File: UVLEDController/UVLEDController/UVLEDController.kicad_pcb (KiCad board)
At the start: 2 copper layers, 56 x 80 mm, 13 parts, among them J1-LED1 Screw_Terminal_01x02, J2-PWR1 Screw_Terminal_01x02, J3 Conn_01x04_Male, Q1 Q_NMOS_GDS

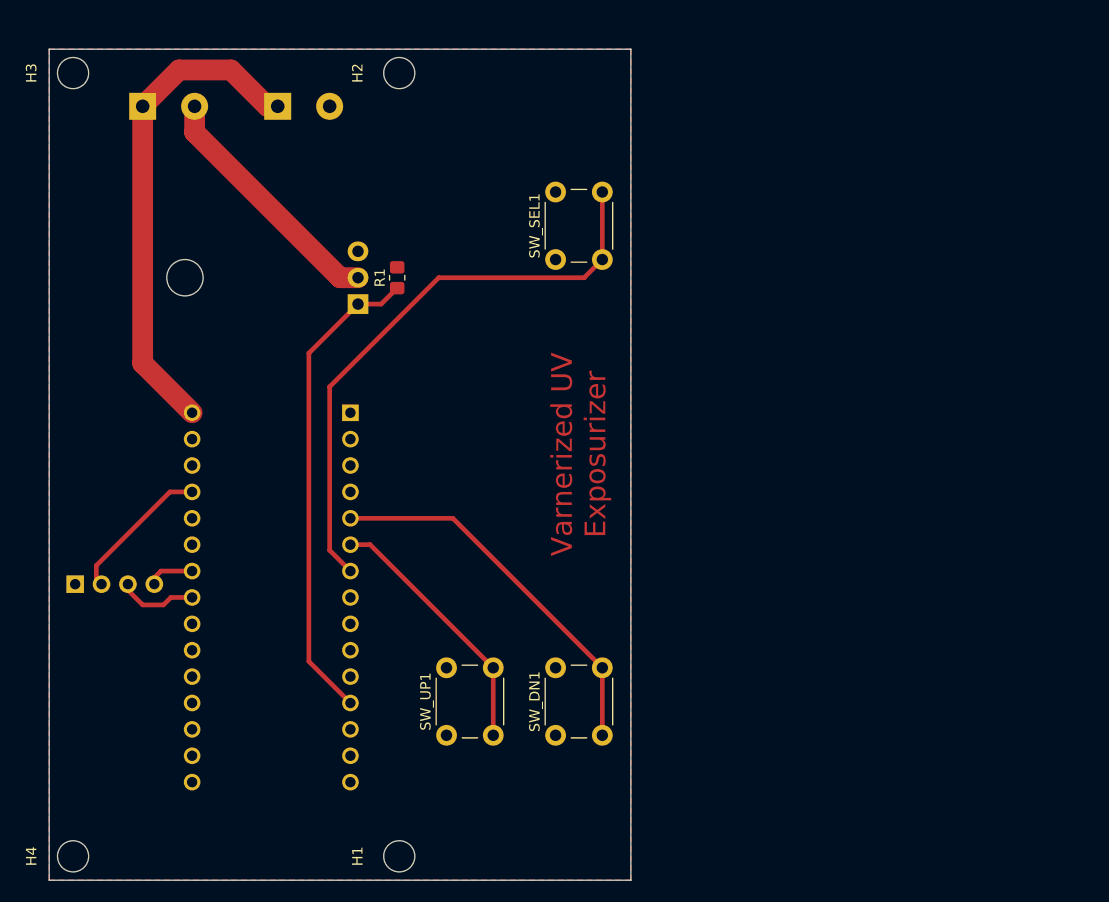
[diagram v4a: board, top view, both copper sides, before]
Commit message: MOved the drill and place offset.
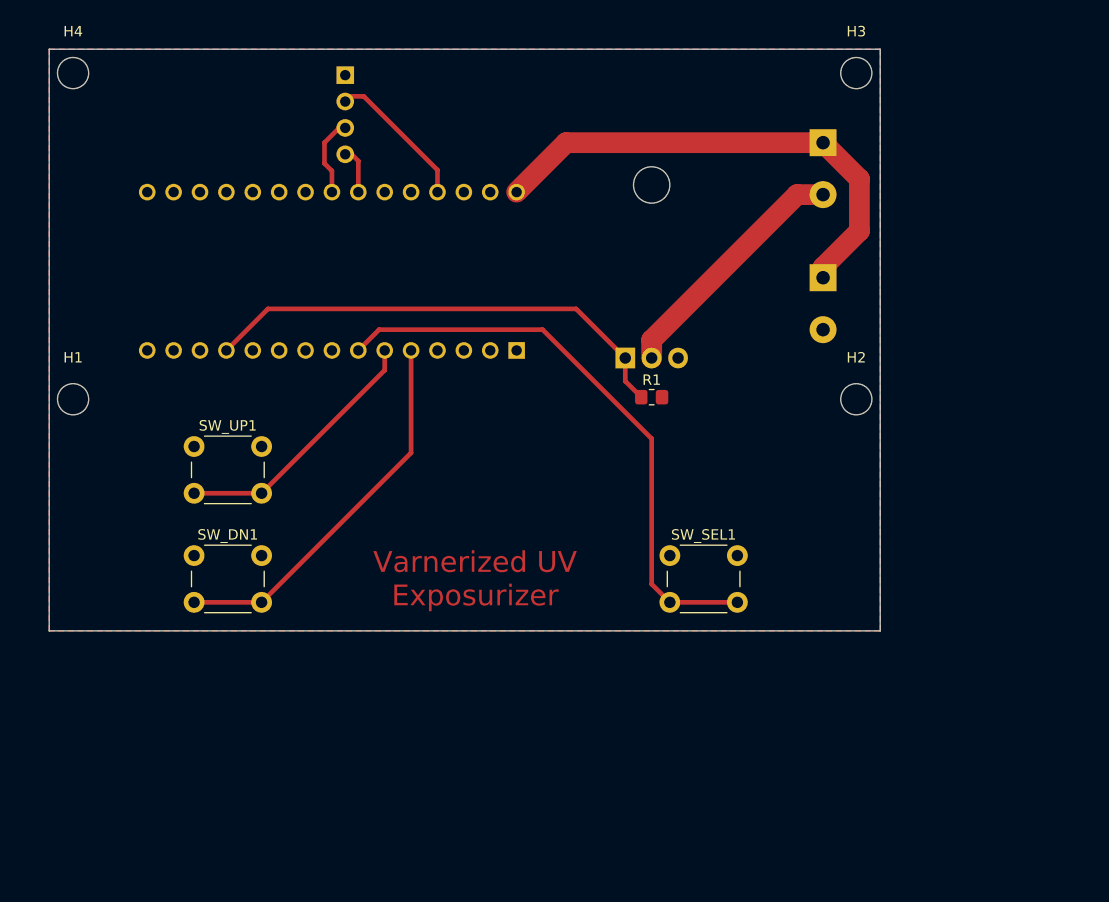
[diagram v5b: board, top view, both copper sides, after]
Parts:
- moved H4 75.4 mm to (122.3, 32.3), turned to 0 degrees
- moved H3 75.4 mm to (197.7, 32.3), turned to 0 degrees
- moved J1-LED1 65.6 mm to (194.5, 39.0), turned to -90 degrees
- moved J3 55.5 mm to (148.5, 32.5), turned to 180 degrees
- moved J2-PWR1 55.0 mm to (194.5, 52.0), turned to -90 degrees
- moved H1 54.1 mm to (122.3, 63.7), turned to 0 degrees
- moved H2 54.1 mm to (197.7, 63.7), turned to 0 degrees
- moved SW_DN1 38.9 mm to (133.9, 78.8), turned to 0 degrees
- moved SW_UP1 36.9 mm to (133.9, 68.2), turned to 0 degrees
- moved SW_SEL1 30.5 mm to (179.8, 78.8), turned to 0 degrees
- moved R1 27.1 mm to (178.0, 63.5), turned to 0 degrees
- moved Q1 26.2 mm to (175.5, 59.7), turned to 0 degrees
- moved A1 17.1 mm to (165.0, 59.0), turned to 90 degrees
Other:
- board size 56 x 80 mm -> 80 x 56 mm
